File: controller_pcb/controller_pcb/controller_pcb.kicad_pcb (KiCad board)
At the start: 2 copper layers, 34 parts, among them J1 USB_B_Micro, Y1 8MHz

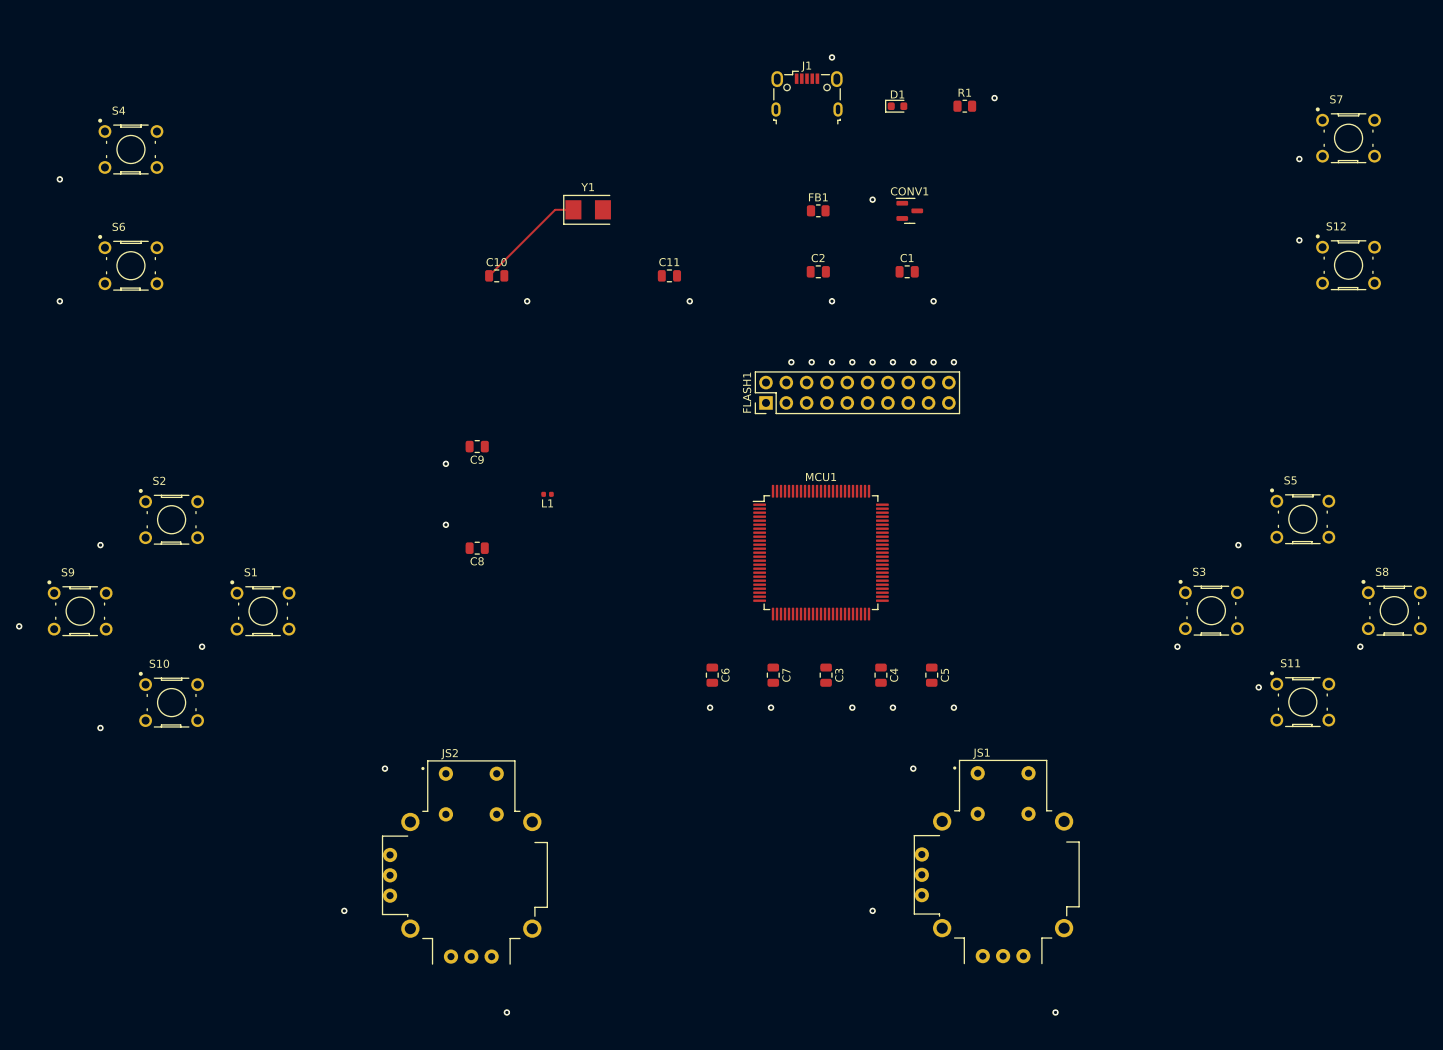
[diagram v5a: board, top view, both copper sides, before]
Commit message: Created GND layer correctly
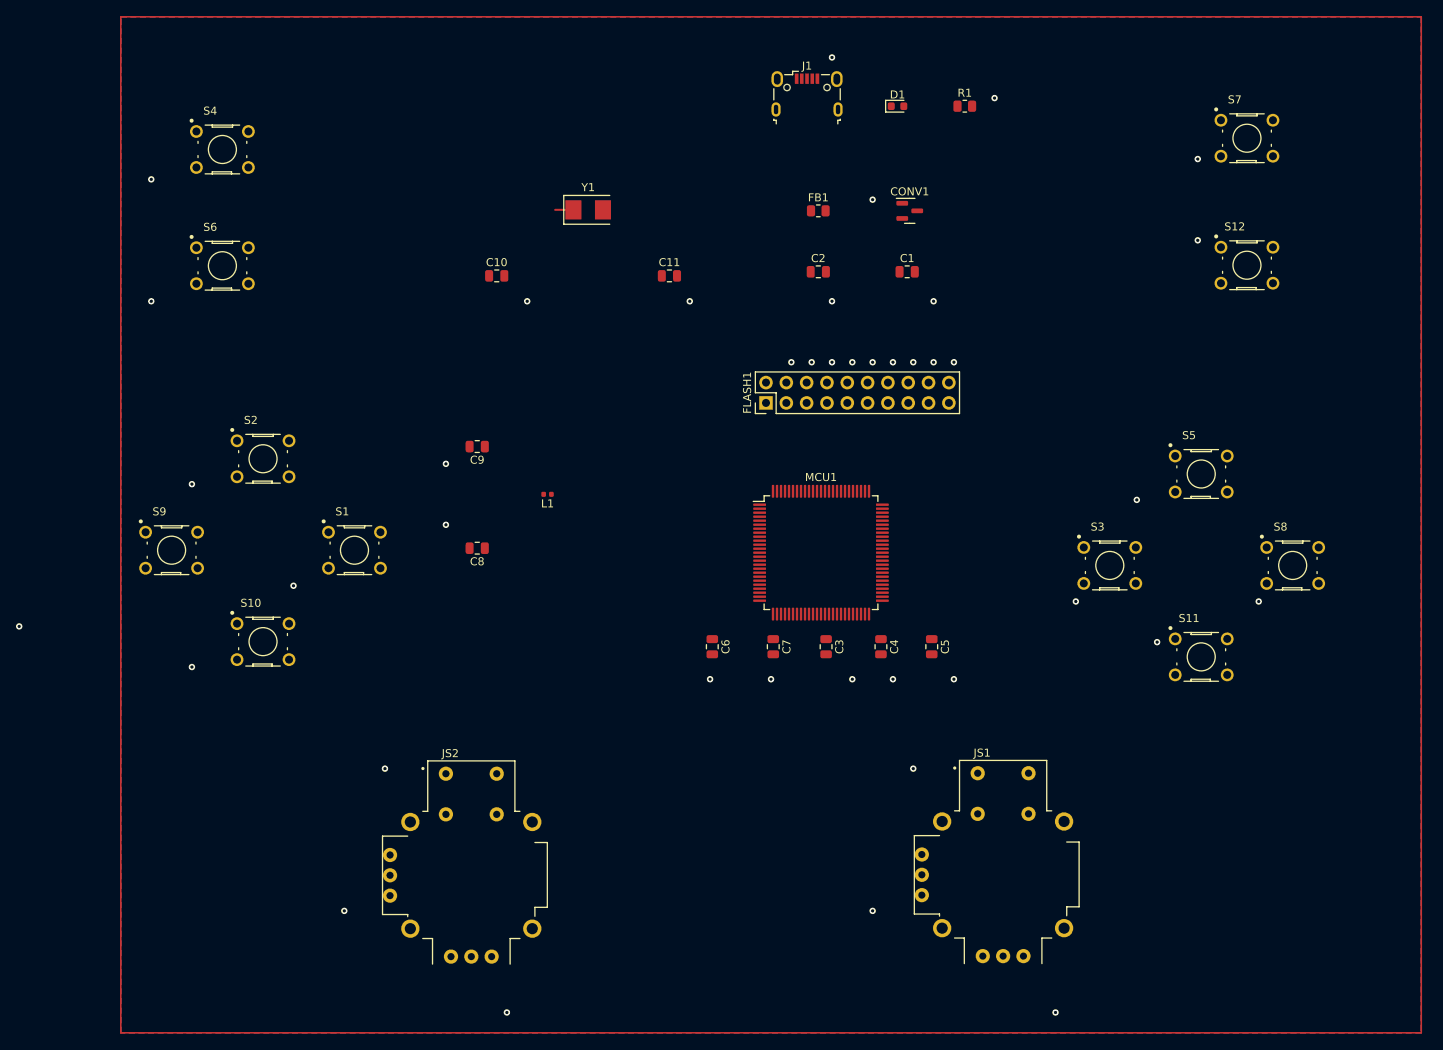
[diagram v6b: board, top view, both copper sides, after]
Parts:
- moved S8 13.9 mm to (217.6, 106.7)
- moved S11 13.9 mm to (206.2, 118.1)
- moved S3 13.9 mm to (194.7, 106.7)
- moved S5 13.9 mm to (206.2, 95.2)
- moved S10 13.7 mm to (88.9, 116.2)
- moved S2 13.7 mm to (88.9, 93.3)
- moved S1 13.7 mm to (100.3, 104.8)
- moved S9 13.7 mm to (77.5, 104.8)
- moved S12 12.7 mm to (211.9, 69.2)
- moved S7 12.7 mm to (211.9, 53.3)
- moved S4 11.4 mm to (83.8, 54.7)
- moved S6 11.4 mm to (83.8, 69.2)
- moved C3 3.56 mm to (159.3, 116.8)
- moved C4 3.56 mm to (166.1, 116.8)
- moved C5 3.56 mm to (172.5, 116.8)
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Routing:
- net Net-(MCU1-Pad12): track 13.9 -> 2.27 mm
- added copper zone on B.Cu, net GND
- added copper zone on F.Cu, net GND

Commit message: did some stuff
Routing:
- net USB_DM: track 0.00 -> 80.6 mm, vias 0 -> 2
- net +5V: track 0.00 -> 50.9 mm
- net (no net): vias 41 -> 40
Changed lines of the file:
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@@
   (via (at 121.92 73.66) (size 0.8) (drill 0.4) (layers "F.Cu" "B.Cu") (free) (net 0))
   (via (at 160.02 81.28) (size 0.8) (drill 0.4) (layers "F.Cu" "B.Cu") (free) (net 0))
-  (via (at 58.42 114.3) (size 0.8) (drill 0.4) (layers "F.Cu" "B.Cu") (free) (net 0))
   (via (at 111.76 101.6) (size 0.8) (drill 0.4) (layers "F.Cu" "B.Cu") (free) (net 0))
   (via (at 190.5 111.187154) (size 0.8) (drill 0.4) (layers "F.Cu" "B.Cu") (free) (net 0))
@@
   (via (at 80.01 119.38) (size 0.8) (drill 0.4) (layers "F.Cu" "B.Cu") (free) (net 0))
   (via (at 170.18 81.28) (size 0.8) (drill 0.4) (layers "F.Cu" "B.Cu") (free) (net 0))
+  (segment (start 154.94 58.42) (end 157.48 58.42) (width 0.25) (layer "F.Cu") (net 6))
+  (segment (start 157.48 58.42) (end 159.2205 60.1605) (width 0.25) (layer "F.Cu") (net 6))
+  (segment (start 144.78 48.26) (end 154.94 58.42) (width 0.25) (layer "F.Cu") (net 6))
+  (segment (start 210.82 45.72) (end 213.36 45.72) (width 0.25) (layer "F.Cu") (net 6))
+  (segment (start 210.82 40.64) (end 210.82 45.72) (width 0.25) (layer "F.Cu") (net 6))
+  (segment (start 154.94 40.64) (end 147.32 40.64) (width 0.25) (layer "F.Cu") (net 6))
+  (segment (start 159.2205 60.1605) (end 159.2205 62.357) (width 0.25) (layer "F.Cu") (net 6))
+  (segment (start 147.32 40.64) (end 144.78 43.18) (width 0.25) (layer "F.Cu") (net 6))
+  (segment (start 155.599 45.836) (end 155.599 41.299) (width 0.25) (layer "F.Cu") (net 6))
+  (segment (start 144.78 43.18) (end 144.78 48.26) (width 0.25) (layer "F.Cu") (net 6))
+  (segment (start 155.599 41.299) (end 154.94 40.64) (width 0.25) (layer "F.Cu") (net 6))
+  (segment (start 166.337 101.6) (end 166.321 101.584) (width 0.25) (layer "F.Cu") (net 7))
+  (segment (start 170.18 101.6) (end 166.337 101.6) (width 0.25) (layer "F.Cu") (net 7))
+  (segment (start 156.249 44.411) (end 160.02 40.64) (width 0.25) (layer "F.Cu") (net 7))
+  (segment (start 156.249 45.836) (end 156.249 44.411) (width 0.25) (layer "F.Cu") (net 7))
+  (via (at 160.02 40.64) (size 0.8) (drill 0.4) (layers "F.Cu" "B.Cu") (net 7))
+  (via (at 170.18 101.6) (size 0.8) (drill 0.4) (layers "F.Cu" "B.Cu") (net 7))
+  (segment (start 175.984511 56.604511) (end 175.984511 93.98) (width 0.25) (layer "B.Cu") (net 7))
+  (segment (start 160.02 40.64) (end 175.984511 56.604511) (width 0.25) (layer "B.Cu") (net 7))
+  (segment (start 175.984511 93.98) (end 170.18 99.784511) (width 0.25) (layer "B.Cu") (net 7))
+  (segment (start 170.18 99.784511) (end 170.18 101.6) (width 0.25) (layer "B.Cu") (net 7))
   (segment (start 127.69 62.23) (end 125.415 62.23) (width 0.25) (layer "F.Cu") (net 11))
   (zone (net 2) (net_name "GND") (layers F&B.Cu) (name "GND") (hatch edge 0.508)
